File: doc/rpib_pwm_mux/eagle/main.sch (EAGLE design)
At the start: 21 parts, among them T1 2N2222, T10 2N2222, T11 2N2222, T7 2N2222, T8 2N2222, T9 2N2222

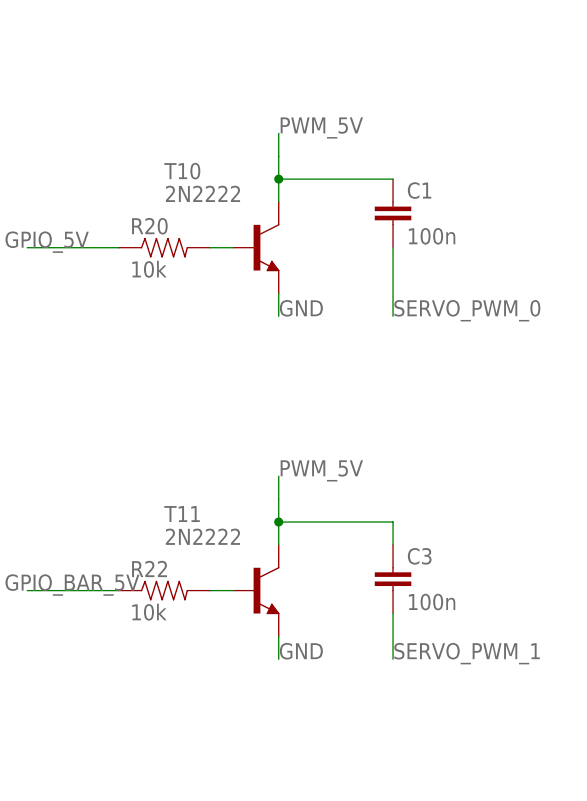
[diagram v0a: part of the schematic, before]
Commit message: [ fix ] rpib_pwm_mux eagle
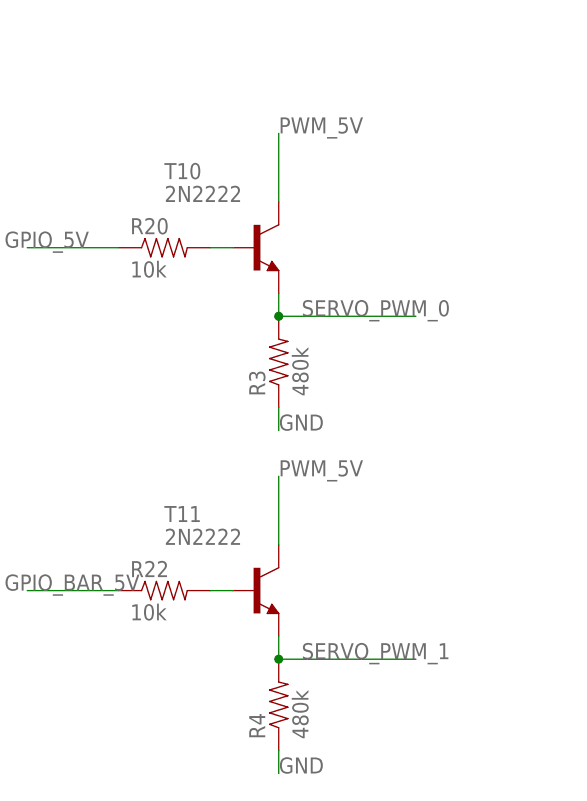
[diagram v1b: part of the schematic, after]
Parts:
- removed C1, C3: 100n, SparkFun:CAPPTH1
- added R3, R4: 480k, SparkFun:RESISTORPTH-1/4W
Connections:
- net GND: now also R3.1, R4.1; no longer T10.E, T11.E
- net GPIO_5V: no longer C1.1, T10.C
- net PWM_5V: now also T10.C; no longer C3.1
- net SERVO_PWM_0: now also R3.2, T10.E; no longer C1.2
- net SERVO_PWM_1: now also R4.2, T11.E; no longer C3.2
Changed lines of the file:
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@@
 <part name="R1" library="SparkFun" deviceset="RESISTOR" device="PTH-1/4W" value="100"/>
 <part name="R2" library="SparkFun" deviceset="RESISTOR" device="PTH-1/4W" value="100"/>
-<part name="C1" library="SparkFun" deviceset="CAP" device="PTH1" value="100n"/>
 <part name="JP1" library="SparkFun" deviceset="M04" device="LONGPADS"/>
 <part name="T7" library="transistor" deviceset="2N2222" device=""/>
@@
 <part name="T11" library="transistor" deviceset="2N2222" device=""/>
 <part name="R22" library="SparkFun" deviceset="RESISTOR" device="PTH-1/4W" value="10k"/>
-<part name="C3" library="SparkFun" deviceset="CAP" device="PTH1" value="100n"/>
 <part name="JP2" library="SparkFun" deviceset="M03" device="LONGPADS"/>
 <part name="JP3" library="SparkFun" deviceset="M03" device="LONGPADS"/>
+<part name="R3" library="SparkFun" deviceset="RESISTOR" device="PTH-1/4W" value="480k"/>
+<part name="R4" library="SparkFun" deviceset="RESISTOR" device="PTH-1/4W" value="480k"/>
 </parts>
 <sheets>
@@
 <instance part="R1" gate="G$1" x="38.1" y="40.64" rot="R90"/>
 <instance part="R2" gate="G$1" x="25.4" y="25.4"/>
-<instance part="C1" gate="G$1" x="154.94" y="27.94"/>
 <instance part="JP1" gate="G$1" x="-12.7" y="10.16"/>
 <instance part="T7" gate="G$1" x="35.56" y="-12.7"/>
@@
 <instance part="T11" gate="G$1" x="139.7" y="-12.7"/>
 <instance part="R22" gate="G$1" x="129.54" y="-12.7"/>
-<instance part="C3" gate="G$1" x="154.94" y="-12.7"/>
 <instance part="JP2" gate="G$1" x="-15.24" y="-5.08"/>
 <instance part="JP3" gate="G$1" x="-15.24" y="-20.32"/>
+<instance part="R3" gate="G$1" x="142.24" y="12.7" rot="R90"/>
+<instance part="R4" gate="G$1" x="142.24" y="-25.4" rot="R90"/>
 </instances>
 <busses>
@@
 </segment>
 <segment>
-<pinref part="T10" gate="G$1" pin="E"/>
-<wire x1="142.24" y1="20.32" x2="142.24" y2="17.78" width="0.1524" layer="91"/>
-<label x="142.24" y="17.78" size="1.778" layer="95"/>
-</segment>
-<segment>
-<pinref part="T11" gate="G$1" pin="E"/>
-<wire x1="142.24" y1="-17.78" x2="142.24" y2="-20.32" width="0.1524" layer="91"/>
-<label x="142.24" y="-20.32" size="1.778" layer="95"/>
-</segment>
-<segment>
 <pinref part="JP2" gate="G$1" pin="3"/>
 <wire x1="-7.62" y1="-2.54" x2="5.08" y2="-2.54" width="0.1524" layer="91"/>
@@
 <wire x1="-7.62" y1="-17.78" x2="5.08" y2="-17.78" width="0.1524" layer="91"/>
 <label x="-7.62" y="-17.78" size="1.778" layer="95"/>
+</segment>
+<segment>
+<pinref part="R3" gate="G$1" pin="1"/>
+<wire x1="142.24" y1="7.62" x2="142.24" y2="5.08" width="0.1524" layer="91"/>
+<label x="142.24" y="5.08" size="1.778" layer="95"/>
+</segment>
+<segment>
+<pinref part="R4" gate="G$1" pin="1"/>
+<wire x1="142.24" y1="-30.48" x2="142.24" y2="-33.02" width="0.1524" layer="91"/>
+<label x="142.24" y="-33.02" size="1.778" layer="95"/>
 </segment>
 </net>
@@
 </segment>
 <segment>
-<pinref part="T10" gate="G$1" pin="C"/>
-<wire x1="142.24" y1="35.56" x2="142.24" y2="33.02" width="0.1524" layer="91"/>
-<pinref part="C1" gate="G$1" pin="1"/>
-<wire x1="142.24" y1="33.02" x2="142.24" y2="30.48" width="0.1524" layer="91"/>
-<wire x1="142.24" y1="33.02" x2="154.94" y2="33.02" width="0.1524" layer="91"/>
-<junction x="142.24" y="33.02"/>
-</segment>
-<segment>
 <pinref part="R20" gate="G$1" pin="1"/>
 <wire x1="124.46" y1="25.4" x2="114.3" y2="25.4" width="0.1524" layer="91"/>
@@
 </segment>
 <segment>
+<pinref part="T10" gate="G$1" pin="C"/>
+<wire x1="142.24" y1="30.48" x2="142.24" y2="38.1" width="0.1524" layer="91"/>
+<label x="142.24" y="38.1" size="1.778" layer="95"/>
+</segment>
+<segment>
 <pinref part="T11" gate="G$1" pin="C"/>
-<wire x1="142.24" y1="-2.54" x2="142.24" y2="-5.08" width="0.1524" layer="91"/>
-<wire x1="142.24" y1="-5.08" x2="142.24" y2="-7.62" width="0.1524" layer="91"/>
-<wire x1="142.24" y1="-5.08" x2="154.94" y2="-5.08" width="0.1524" layer="91"/>
-<junction x="142.24" y="-5.08"/>
-<wire x1="154.94" y1="-5.08" x2="154.94" y2="-7.62" width="0.1524" layer="91"/>
-<pinref part="C3" gate="G$1" pin="1"/>
-</segment>
-<segment>
-<wire x1="142.24" y1="35.56" x2="142.24" y2="38.1" width="0.1524" layer="91"/>
-<label x="142.24" y="38.1" size="1.778" layer="95"/>
-</segment>
-<segment>
-<wire x1="142.24" y1="-2.54" x2="142.24" y2="0" width="0.1524" layer="91"/>
+<wire x1="142.24" y1="-7.62" x2="142.24" y2="0" width="0.1524" layer="91"/>
 <label x="142.24" y="0" size="1.778" layer="95"/>
 </segment>
@@
 <net name="SERVO_PWM_0" class="0">
 <segment>
-<pinref part="C1" gate="G$1" pin="2"/>
-<wire x1="154.94" y1="25.4" x2="154.94" y2="17.78" width="0.1524" layer="91"/>
-<label x="154.94" y="17.78" size="1.778" layer="95"/>
-</segment>
-<segment>
 <pinref part="JP2" gate="G$1" pin="1"/>
 <wire x1="-7.62" y1="-7.62" x2="5.08" y2="-7.62" width="0.1524" layer="91"/>
 <label x="-7.62" y="-7.62" size="1.778" layer="95"/>
 </segment>
+<segment>
+<pinref part="T10" gate="G$1" pin="E"/>
+<pinref part="R3" gate="G$1" pin="2"/>
+<wire x1="142.24" y1="20.32" x2="142.24" y2="17.78" width="0.1524" layer="91"/>
+<wire x1="142.24" y1="17.78" x2="157.48" y2="17.78" width="0.1524" layer="91"/>
+<junction x="142.24" y="17.78"/>
+<label x="144.78" y="17.78" size="1.778" layer="95"/>
+</segment>
 </net>
 <net name="SERVO_PWM_1" class="0">
@@
 </segment>
 <segment>
-<pinref part="C3" gate="G$1" pin="2"/>
-<wire x1="154.94" y1="-15.24" x2="154.94" y2="-20.32" width="0.1524" layer="91"/>
-<label x="154.94" y="-20.32" size="1.778" layer="95"/>
-</segment>
-</net>
+<pinref part="T11" gate="G$1" pin="E"/>
+<pinref part="R4" gate="G$1" pin="2"/>
+<wire x1="142.24" y1="-17.78" x2="142.24" y2="-20.32" width="0.1524" layer="91"/>
+<wire x1="142.24" y1="-20.32" x2="157.48" y2="-20.32" width="0.1524" layer="91"/>
+<junction x="142.24" y="-20.32"/>
+<label x="144.78" y="-20.32" size="1.778" layer="95"/>
+</segment>
+</net>

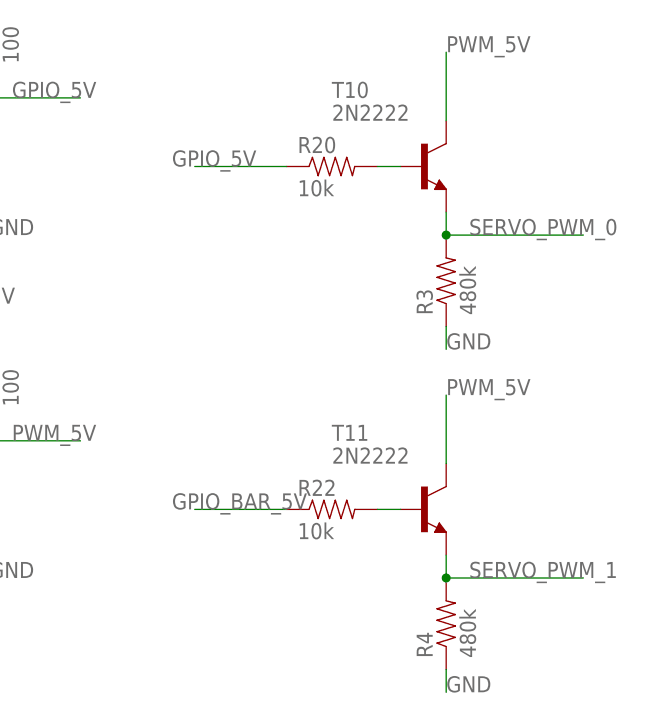
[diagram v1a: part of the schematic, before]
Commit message: [ update ] rpib_pwm_mux schematics, include capa to remove spikes
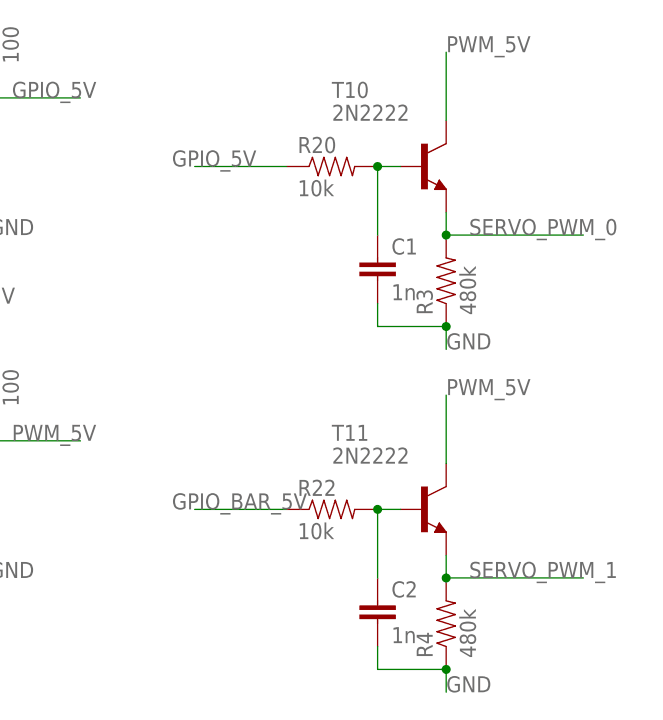
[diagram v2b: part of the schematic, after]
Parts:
- added C1, C2: 1n, SparkFun:CAPKIT
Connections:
- net GND: now also C1.2, C2.2
- net N$5: now also C1.1
- net N$6: now also C2.1
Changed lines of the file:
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@@
 <part name="R3" library="SparkFun" deviceset="RESISTOR" device="PTH-1/4W" value="480k"/>
 <part name="R4" library="SparkFun" deviceset="RESISTOR" device="PTH-1/4W" value="480k"/>
+<part name="C1" library="SparkFun" deviceset="CAP" device="KIT" value="1n"/>
+<part name="C2" library="SparkFun" deviceset="CAP" device="KIT" value="1n"/>
 </parts>
 <sheets>
@@
 <instance part="R3" gate="G$1" x="142.24" y="12.7" rot="R90"/>
 <instance part="R4" gate="G$1" x="142.24" y="-25.4" rot="R90"/>
+<instance part="C1" gate="G$1" x="134.62" y="12.7"/>
+<instance part="C2" gate="G$1" x="134.62" y="-25.4"/>
 </instances>
 <busses>
@@
 <wire x1="142.24" y1="7.62" x2="142.24" y2="5.08" width="0.1524" layer="91"/>
 <label x="142.24" y="5.08" size="1.778" layer="95"/>
+<pinref part="C1" gate="G$1" pin="2"/>
+<wire x1="134.62" y1="10.16" x2="134.62" y2="7.62" width="0.1524" layer="91"/>
+<wire x1="134.62" y1="7.62" x2="142.24" y2="7.62" width="0.1524" layer="91"/>
+<junction x="142.24" y="7.62"/>
 </segment>
 <segment>
@@
 <wire x1="142.24" y1="-30.48" x2="142.24" y2="-33.02" width="0.1524" layer="91"/>
 <label x="142.24" y="-33.02" size="1.778" layer="95"/>
+<pinref part="C2" gate="G$1" pin="2"/>
+<wire x1="134.62" y1="-27.94" x2="134.62" y2="-30.48" width="0.1524" layer="91"/>
+<wire x1="134.62" y1="-30.48" x2="142.24" y2="-30.48" width="0.1524" layer="91"/>
+<junction x="142.24" y="-30.48"/>
 </segment>
 </net>
@@
 <pinref part="T10" gate="G$1" pin="B"/>
 <wire x1="134.62" y1="25.4" x2="137.16" y2="25.4" width="0.1524" layer="91"/>
+<pinref part="C1" gate="G$1" pin="1"/>
+<wire x1="134.62" y1="25.4" x2="134.62" y2="17.78" width="0.1524" layer="91"/>
+<junction x="134.62" y="25.4"/>
 </segment>
 </net>
@@
 <pinref part="T11" gate="G$1" pin="B"/>
 <wire x1="134.62" y1="-12.7" x2="137.16" y2="-12.7" width="0.1524" layer="91"/>
-</segment>
-</net>
+<pinref part="C2" gate="G$1" pin="1"/>
+<wire x1="134.62" y1="-12.7" x2="134.62" y2="-20.32" width="0.1524" layer="91"/>
+<junction x="134.62" y="-12.7"/>
+</segment>
+</net>
